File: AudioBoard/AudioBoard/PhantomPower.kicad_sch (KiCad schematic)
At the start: 1 part, among them SW2 SW_SPDT_321

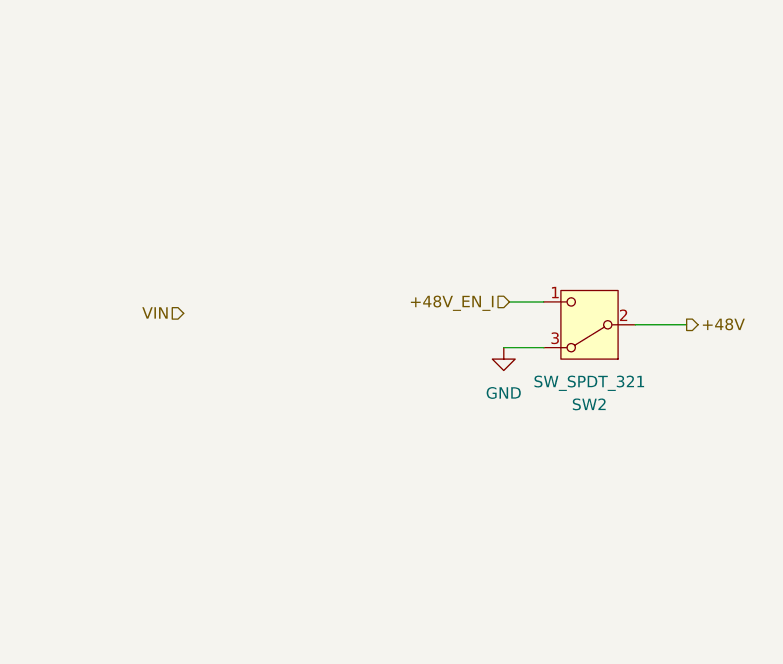
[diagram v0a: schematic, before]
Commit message: added power electronics
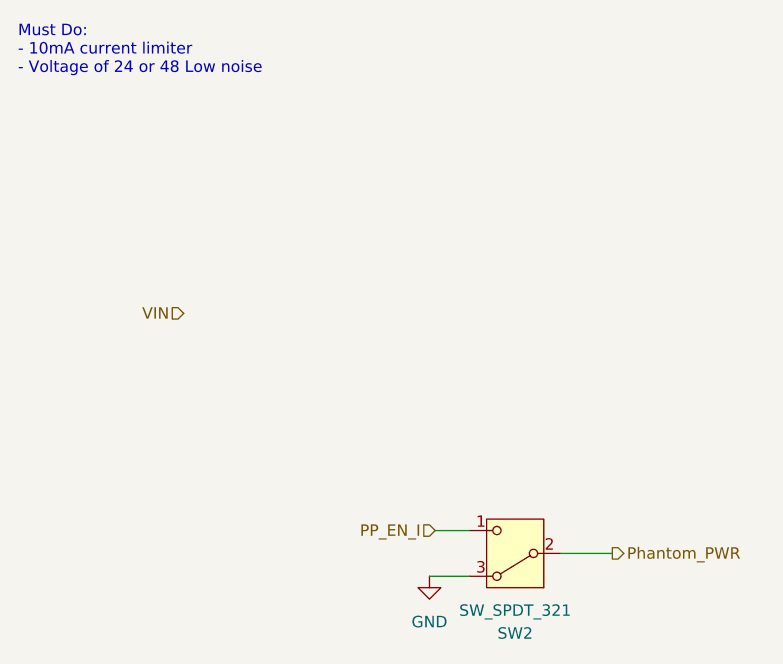
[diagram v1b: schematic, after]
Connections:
- net +48V renamed Phantom_PWR
- net +48V_EN_I renamed PP_EN_I
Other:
- note added: "Must Do: - 10mA current limiter - Voltage of 24 or 48 Low noise"
- moved on the sheet: SW2
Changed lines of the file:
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@@
 	(generator_version "10.0")
 	(paper "A4")
+	(text "Must Do:\n- 10mA current limiter\n- Voltage of 24 or 48 Low noise"
+		(exclude_from_sim no)
+		(at 27.305 31.115 0)
+		(effects
+			(font
+				(size 1.27 1.27)
+			)
+			(justify left)
+		)
+	)
 	(wire
 		(pts
-			(xy 101.6 61.595) (xy 95.885 61.595)
+			(xy 93.345 86.995) (xy 87.63 86.995)
 		)
 		(stroke
@@
 	(wire
 		(pts
-			(xy 81.28 64.135) (xy 85.725 64.135)
+			(xy 73.025 89.535) (xy 77.47 89.535)
 		)
 		(stroke
@@
 	(wire
 		(pts
-			(xy 81.915 59.055) (xy 85.725 59.055)
+			(xy 73.66 84.455) (xy 77.47 84.455)
 		)
 		(stroke
@@
 		)
 	)
-	(hierarchical_label "+48V_EN_I"
+	(hierarchical_label "Phantom_PWR"
+		(shape output)
+		(at 93.345 86.995 0)
+		(effects
+			(font
+				(size 1.27 1.27)
+			)
+			(justify left)
+		)
+	)
+	(hierarchical_label "PP_EN_I"
 		(shape input)
-		(at 81.915 59.055 180)
+		(at 73.66 84.455 180)
 		(effects
 			(font
@@
 			)
 			(justify right)
-		)
-	)
-	(hierarchical_label "+48V"
-		(shape output)
-		(at 101.6 61.595 0)
-		(effects
-			(font
-				(size 1.27 1.27)
-			)
-			(justify left)
 		)
 	)
@@
 	(symbol
 		(lib_id "Switch:SW_SPDT_321")
-		(at 90.805 61.595 180)
+		(at 82.55 86.995 180)
 		(unit 1)
 		(body_style 1)
@@
 		(fields_autoplaced yes)
 		(property "Reference" "SW2"
-			(at 90.805 70.485 0)
+			(at 82.55 95.885 0)
 			(show_name no)
 			(do_not_autoplace no)
@@
 		)
 		(property "Value" "SW_SPDT_321"
-			(at 90.805 67.945 0)
+			(at 82.55 93.345 0)
 			(show_name no)
 			(do_not_autoplace no)
@@
 		)
 		(property "Footprint" "haoyu:SS-12D28G7"
-			(at 90.805 51.435 0)
+			(at 82.55 76.835 0)
 			(hide yes)
 			(show_name no)
@@
 		)
 		(property "Datasheet" ""
-			(at 90.805 53.975 0)
+			(at 82.55 79.375 0)
 			(hide yes)
 			(show_name no)
@@
 		)
 		(property "Description" "Switch, single pole double throw"
-			(at 90.805 61.595 0)
+			(at 82.55 86.995 0)
 			(hide yes)
 			(show_name no)
@@
 		)
 		(property "jlcpcbpart" "C2884748"
-			(at 90.805 61.595 0)
+			(at 82.55 86.995 0)
 			(hide yes)
 			(show_name no)
@@
 		)
 		(property "JLCPCB" "C2884748"
-			(at 90.805 61.595 0)
+			(at 82.55 86.995 0)
 			(hide yes)
 			(show_name no)
@@
 		)
 		(property "LCSC Part" "C2884748"
-			(at 90.805 61.595 0)
+			(at 82.55 86.995 0)
 			(hide yes)
 			(show_name no)
@@
 	(symbol
 		(lib_id "power:GND")
-		(at 81.28 64.135 0)
+		(at 73.025 89.535 0)
 		(unit 1)
 		(body_style 1)
@@
 		(fields_autoplaced yes)
 		(property "Reference" "#PWR088"
-			(at 81.28 70.485 0)
+			(at 73.025 95.885 0)
 			(hide yes)
 			(show_name no)
@@
 		)
 		(property "Value" "GND"
-			(at 81.28 69.215 0)
+			(at 73.025 94.615 0)
 			(show_name no)
 			(do_not_autoplace no)
@@
 		)
 		(property "Footprint" ""
-			(at 81.28 64.135 0)
+			(at 73.025 89.535 0)
 			(hide yes)
 			(show_name no)
@@
 		)
 		(property "Datasheet" ""
-			(at 81.28 64.135 0)
+			(at 73.025 89.535 0)
 			(hide yes)
 			(show_name no)
@@
 		)
 		(property "Description" ""
-			(at 81.28 64.135 0)
-			(show_name no)
-			(do_not_autoplace no)
+			(at 73.025 89.535 0)
+			(show_name no)
+			(do_not_autoplace no)
